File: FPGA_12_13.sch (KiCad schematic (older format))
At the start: 2 parts, among them U1 XC7K160T-FFG676, U51 TXB0104D

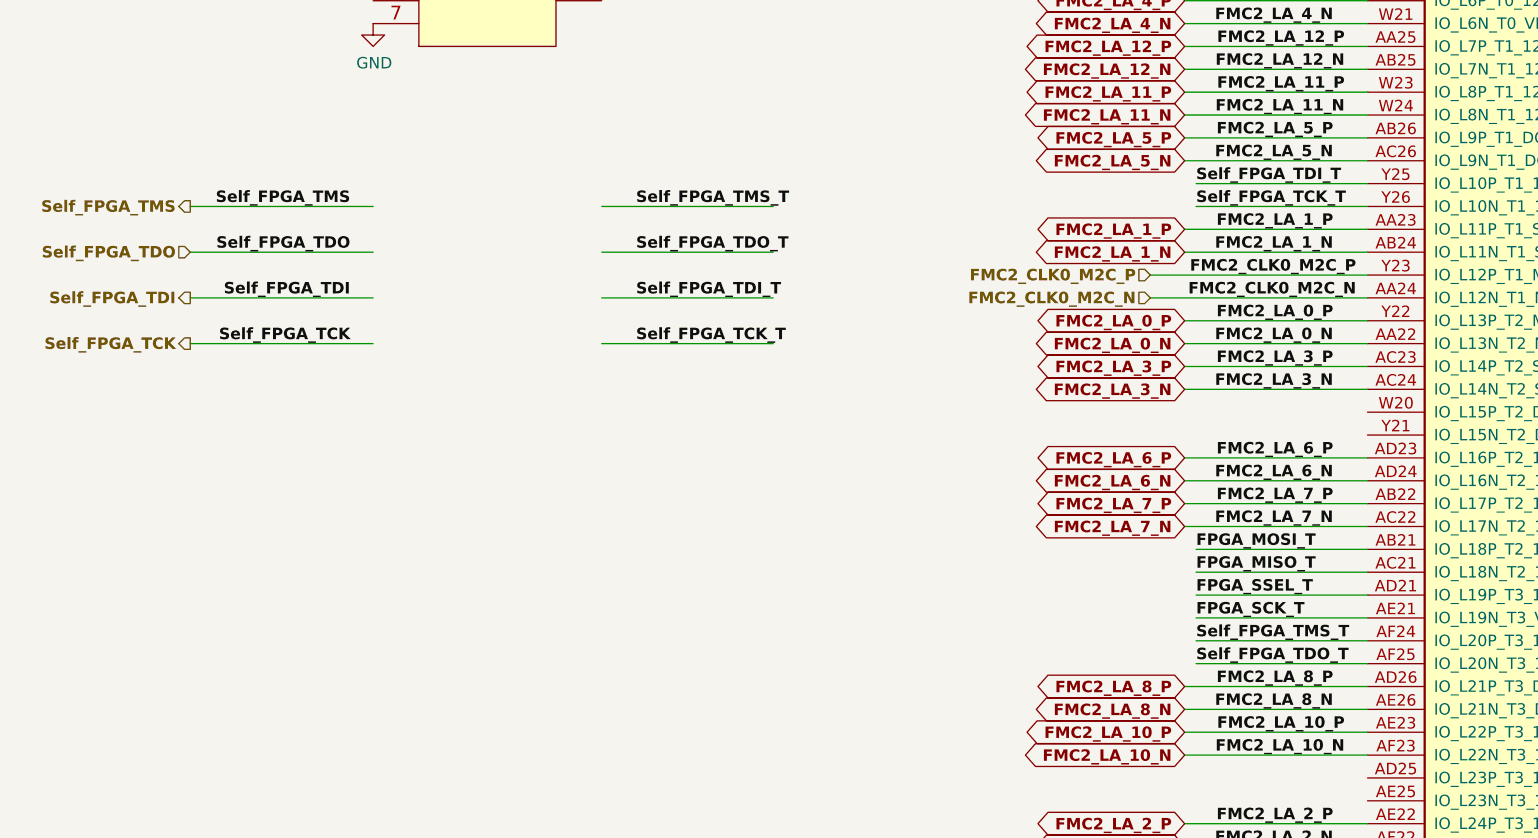
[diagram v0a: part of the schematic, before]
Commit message: MMC routing done
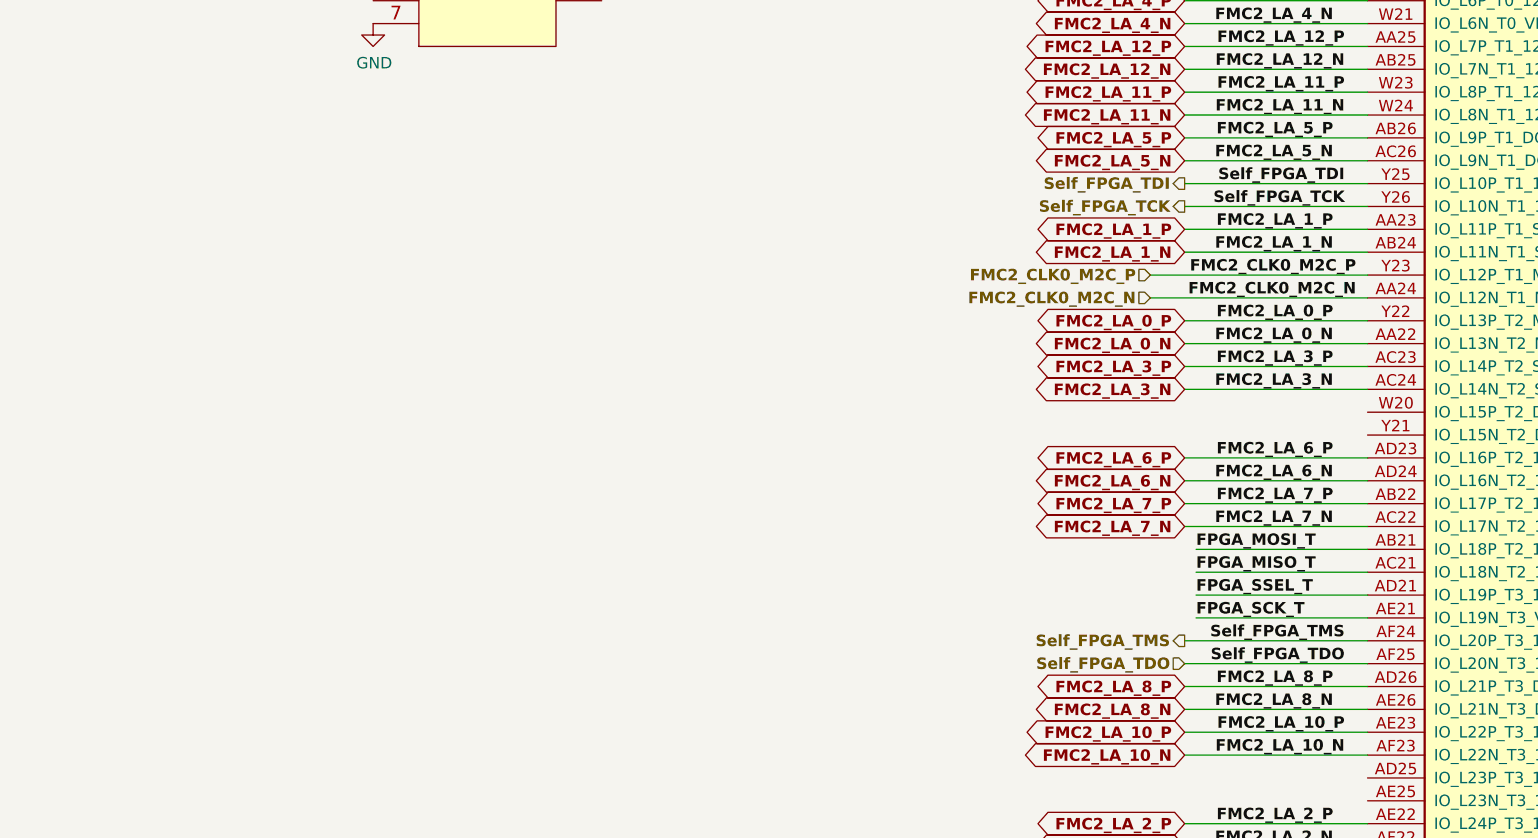
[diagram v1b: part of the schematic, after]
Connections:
- net labels removed: Self_FPGA_TCK_T, Self_FPGA_TDI_T, Self_FPGA_TDO_T, Self_FPGA_TMS_T
- wire segments 165 -> 157
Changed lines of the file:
@@
 Text GLabel 5800 4050 0    50   BiDi ~ 10
 FMC2_LA_16_N
-Text Label 6450 7150 2    50   ~ 10
-FMC2_LA_8_P
 Text Label 6450 7250 2    50   ~ 10
 FMC2_LA_8_N
@@
 Text Label 3400 3950 0    50   ~ 10
 FPGA_SCK_T
-Text Label 3400 5050 0    50   ~ 10
-Self_FPGA_TMS_T
-Text Label 3400 5250 0    50   ~ 10
-Self_FPGA_TDO_T
-Text Label 3400 5450 0    50   ~ 10
-Self_FPGA_TDI_T
-Text Label 3400 5650 0    50   ~ 10
-Self_FPGA_TCK_T
-Wire Wire Line
-	4000 5050 3250 5050
-Wire Wire Line
-	4000 5250 3250 5250
-Wire Wire Line
-	4000 5450 3250 5450
-Wire Wire Line
-	4000 5650 3250 5650
 Wire Wire Line
 	3250 3550 4000 3550
@@
 Text Label 5850 6850 0    50   ~ 10
 FPGA_SCK_T
-Text Label 5850 6950 0    50   ~ 10
-Self_FPGA_TMS_T
-Text Label 5850 7050 0    50   ~ 10
-Self_FPGA_TDO_T
-Text Label 5850 4950 0    50   ~ 10
-Self_FPGA_TDI_T
-Text Label 5850 5050 0    50   ~ 10
-Self_FPGA_TCK_T
-Wire Wire Line
-	6600 6950 5850 6950
-Wire Wire Line
-	6600 7050 5850 7050
-Wire Wire Line
-	6600 4950 5850 4950
-Wire Wire Line
-	6600 5050 5850 5050
 Wire Wire Line
 	5850 6650 6600 6650
@@
 Text HLabel 1450 3350 0    50   Output ~ 10
 FPGA_MOSI
-Text Label 2150 5050 2    50   ~ 10
+Text Label 6500 6950 2    50   ~ 10
 Self_FPGA_TMS
-Text Label 2150 5250 2    50   ~ 10
+Text Label 6500 7050 2    50   ~ 10
 Self_FPGA_TDO
-Text Label 2150 5450 2    50   ~ 10
+Text Label 6500 4950 2    50   ~ 10
 Self_FPGA_TDI
-Text Label 2150 5650 2    50   ~ 10
+Text Label 6500 5050 2    50   ~ 10
 Self_FPGA_TCK
-Text HLabel 1450 5050 0    50   Output ~ 10
+Text HLabel 5800 6950 0    50   Output ~ 10
 Self_FPGA_TMS
-Text HLabel 1450 5250 0    50   Input ~ 10
+Text HLabel 5800 7050 0    50   Input ~ 10
 Self_FPGA_TDO
-Text HLabel 1450 5450 0    50   Output ~ 10
+Text HLabel 5800 4950 0    50   Output ~ 10
 Self_FPGA_TDI
-Text HLabel 1450 5650 0    50   Output ~ 10
+Text HLabel 5800 5050 0    50   Output ~ 10
 Self_FPGA_TCK
 Wire Wire Line
-	1450 5050 2250 5050
-Wire Wire Line
-	1450 5250 2250 5250
-Wire Wire Line
-	1450 5450 2250 5450
-Wire Wire Line
-	1450 5650 2250 5650
+	5800 6950 6600 6950
+Wire Wire Line
+	5800 7050 6600 7050
+Wire Wire Line
+	5800 4950 6600 4950
+Wire Wire Line
+	5800 5050 6600 5050
 Wire Wire Line
 	1450 3350 2250 3350
@@
 	1    0    0    -1
 $EndComp
+Text Label 6450 7150 2    50   ~ 10
+FMC2_LA_8_P
 $EndSCHEMATC

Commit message: clk switch power supply and general routing
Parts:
- added C320, C321: CC0201_100NF_6.3V_10%_X5R, CAPC0603X33N, symbol Capacitors_SMD:CC0201_100NF_6.3V_10%_X5R
- added R8: R0402_0R_JUMPER, Resistors SMD:RESC1005X40N, symbol Resistors_SMD:R0402_0R_JUMPER
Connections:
- net labels added: +3V3
- wire segments 157 -> 166

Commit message: routing done
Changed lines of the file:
@@
 Text Label 6450 5650 2    50   ~ 10
 FMC2_LA_0_N
-Text Label 6450 5750 2    50   ~ 10
+Text Label 6450 7150 2    50   ~ 10
 FMC2_LA_3_P
 Text Label 6450 4750 2    50   ~ 10
@@
 Text Label 6500 3150 2    50   ~ 10
 FMC2_LA_15_P
-Text Label 6450 5850 2    50   ~ 10
+Text Label 6450 7250 2    50   ~ 10
 FMC2_LA_3_N
 Text Label 6450 4850 2    50   ~ 10
@@
 	5800 7850 6600 7850
 Wire Wire Line
-	5800 5750 6600 5750
-Wire Wire Line
-	5800 5850 6600 5850
+	5800 7150 6600 7150
+Wire Wire Line
+	5800 7250 6600 7250
 Wire Wire Line
 	5800 4750 6600 4750
@@
 Text GLabel 5800 7850 0    50   BiDi ~ 10
 FMC2_LA_2_N
-Text GLabel 5800 5750 0    50   BiDi ~ 10
+Text GLabel 5800 7150 0    50   BiDi ~ 10
 FMC2_LA_3_P
-Text GLabel 5800 5850 0    50   BiDi ~ 10
+Text GLabel 5800 7250 0    50   BiDi ~ 10
 FMC2_LA_3_N
 Text GLabel 5800 4750 0    50   BiDi ~ 10
@@
 Text GLabel 5800 4050 0    50   BiDi ~ 10
 FMC2_LA_16_N
-Text Label 6450 7250 2    50   ~ 10
-FMC2_LA_8_N
-Wire Wire Line
-	5800 7150 6600 7150
-Wire Wire Line
-	5800 7250 6600 7250
-Text GLabel 5800 7150 0    50   BiDi ~ 10
-FMC2_LA_8_P
-Text GLabel 5800 7250 0    50   BiDi ~ 10
-FMC2_LA_8_N
 Wire Wire Line
 	5800 3150 6600 3150
@@
 	1    0    0    -1
 $EndComp
-Text Label 6450 7150 2    50   ~ 10
-FMC2_LA_8_P
 $Comp
 L Resistors_SMD:R0402_0R_JUMPER R?
@@
 	3400 4150 3250 4150
 Connection ~ 3400 4150
+Text Label 6450 5850 2    50   ~ 10
+FMC2_LA_8_N
+Wire Wire Line
+	5800 5750 6600 5750
+Wire Wire Line
+	5800 5850 6600 5850
+Text GLabel 5800 5750 0    50   BiDi ~ 10
+FMC2_LA_8_P
+Text GLabel 5800 5850 0    50   BiDi ~ 10
+FMC2_LA_8_N
+Text Label 6450 5750 2    50   ~ 10
+FMC2_LA_8_P
 $EndSCHEMATC

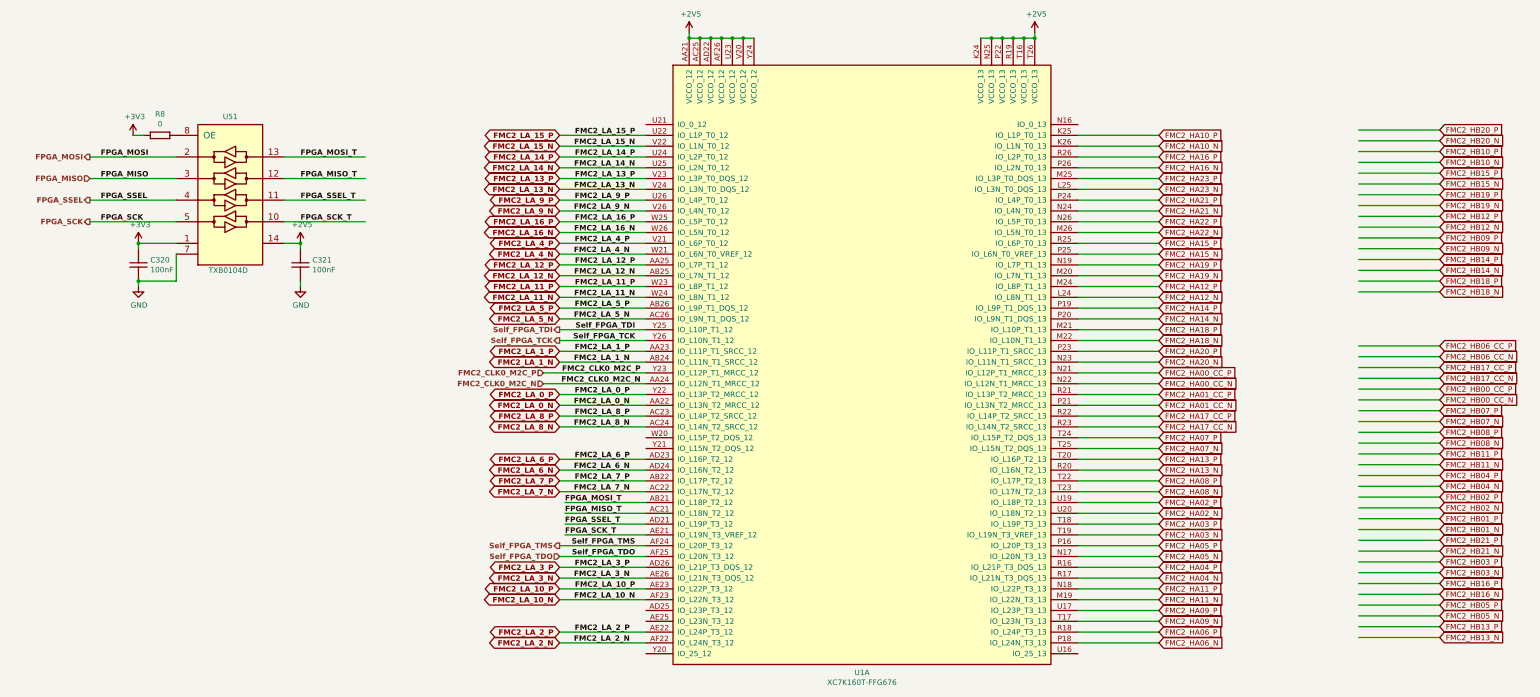
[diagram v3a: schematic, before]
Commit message: DDR lenght mached, 2 additional LEDs added, I2C pullups voltage changed and other minor changes
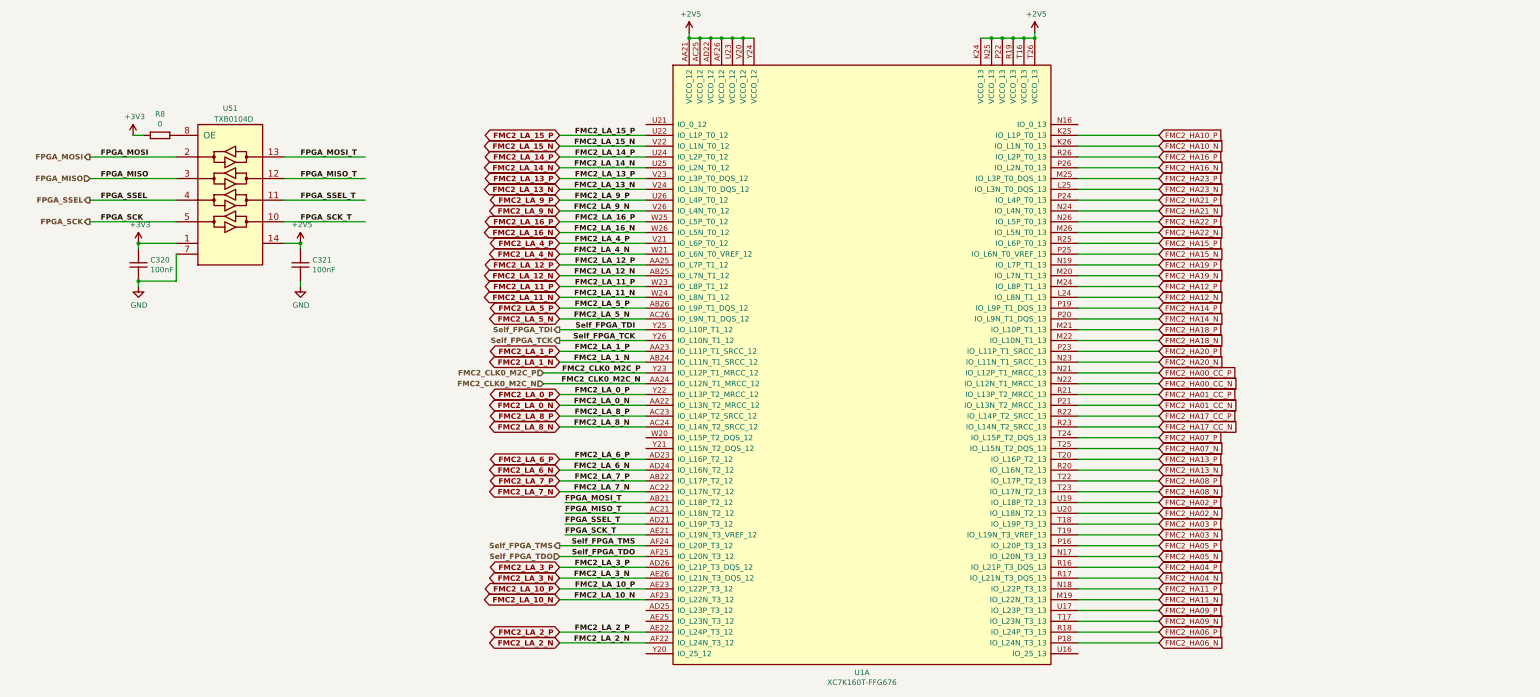
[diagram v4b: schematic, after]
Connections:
- net labels removed: FMC2_HB00_CC_N, FMC2_HB00_CC_P, FMC2_HB01_N, FMC2_HB01_P, FMC2_HB02_N, FMC2_HB02_P, FMC2_HB03_N, FMC2_HB03_P, FMC2_HB04_N, FMC2_HB04_P, FMC2_HB05_N, FMC2_HB05_P, FMC2_HB06_CC_N, FMC2_HB06_CC_P, FMC2_HB07_N, FMC2_HB07_P, FMC2_HB08_N, FMC2_HB08_P, FMC2_HB09_N, FMC2_HB09_P, FMC2_HB10_N, FMC2_HB10_P, FMC2_HB11_N, FMC2_HB11_P, FMC2_HB12_N, FMC2_HB12_P, FMC2_HB13_N, FMC2_HB13_P, FMC2_HB14_N, FMC2_HB14_P, FMC2_HB15_N, FMC2_HB15_P, FMC2_HB16_N, FMC2_HB16_P, FMC2_HB17_CC_N, FMC2_HB17_CC_P, FMC2_HB18_N, FMC2_HB18_P, FMC2_HB19_N, FMC2_HB19_P, FMC2_HB20_N, FMC2_HB20_P, FMC2_HB21_N, FMC2_HB21_P
- wire segments 166 -> 122
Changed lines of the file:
@@
 	1    0    0    -1
 $EndComp
-Wire Wire Line
-	13950 7100 13200 7100
-Wire Wire Line
-	13950 7200 13200 7200
-Wire Wire Line
-	13950 7500 13200 7500
-Wire Wire Line
-	13950 7600 13200 7600
-Wire Wire Line
-	13950 4100 13200 4100
-Wire Wire Line
-	13950 4200 13200 4200
-Wire Wire Line
-	13950 7700 13200 7700
-Wire Wire Line
-	13950 7800 13200 7800
-Wire Wire Line
-	13950 3700 13200 3700
-Wire Wire Line
-	13950 3800 13200 3800
-Text GLabel 13950 7100 2    50   Input ~ 0
-FMC2_HB03_P
-Text GLabel 13950 7200 2    50   Input ~ 0
-FMC2_HB03_N
-Text GLabel 13950 7500 2    50   Input ~ 0
-FMC2_HB05_P
-Text GLabel 13950 7600 2    50   Input ~ 0
-FMC2_HB05_N
-Text GLabel 13950 4100 2    50   Input ~ 0
-FMC2_HB09_P
-Text GLabel 13950 4200 2    50   Input ~ 0
-FMC2_HB09_N
-Text GLabel 13950 7700 2    50   Input ~ 0
-FMC2_HB13_P
-Text GLabel 13950 7800 2    50   Input ~ 0
-FMC2_HB13_N
-Text GLabel 13950 3700 2    50   Input ~ 0
-FMC2_HB19_P
-Text GLabel 13950 3800 2    50   Input ~ 0
-FMC2_HB19_N
-Wire Wire Line
-	13950 6500 13200 6500
-Wire Wire Line
-	13950 6600 13200 6600
-Wire Wire Line
-	13950 6300 13200 6300
-Wire Wire Line
-	13950 6400 13200 6400
-Wire Wire Line
-	13950 5900 13200 5900
-Wire Wire Line
-	13950 6000 13200 6000
-Wire Wire Line
-	13950 3900 13200 3900
-Wire Wire Line
-	13950 4000 13200 4000
-Wire Wire Line
-	13950 7300 13200 7300
-Wire Wire Line
-	13950 7400 13200 7400
-Wire Wire Line
-	13950 3100 13200 3100
-Wire Wire Line
-	13950 3200 13200 3200
-Text GLabel 13950 6500 2    50   Input ~ 0
-FMC2_HB02_P
-Text GLabel 13950 6600 2    50   Input ~ 0
-FMC2_HB02_N
-Text GLabel 13950 6300 2    50   Input ~ 0
-FMC2_HB04_P
-Text GLabel 13950 6400 2    50   Input ~ 0
-FMC2_HB04_N
-Text GLabel 13950 5900 2    50   Input ~ 0
-FMC2_HB08_P
-Text GLabel 13950 6000 2    50   Input ~ 0
-FMC2_HB08_N
-Text GLabel 13950 3900 2    50   Input ~ 0
-FMC2_HB12_P
-Text GLabel 13950 4000 2    50   Input ~ 0
-FMC2_HB12_N
-Text GLabel 13950 7300 2    50   Input ~ 0
-FMC2_HB16_P
-Text GLabel 13950 7400 2    50   Input ~ 0
-FMC2_HB16_N
-Text GLabel 13950 3100 2    50   Input ~ 0
-FMC2_HB20_P
-Text GLabel 13950 3200 2    50   Input ~ 0
-FMC2_HB20_N
-Wire Wire Line
-	13950 6700 13200 6700
-Wire Wire Line
-	13950 6800 13200 6800
-Wire Wire Line
-	13950 5700 13200 5700
-Wire Wire Line
-	13950 5800 13200 5800
-Wire Wire Line
-	13950 6100 13200 6100
-Wire Wire Line
-	13950 6200 13200 6200
-Wire Wire Line
-	13950 3500 13200 3500
-Wire Wire Line
-	13950 3600 13200 3600
-Text GLabel 13950 6700 2    50   Input ~ 0
-FMC2_HB01_P
-Text GLabel 13950 6800 2    50   Input ~ 0
-FMC2_HB01_N
-Text GLabel 13950 5700 2    50   Input ~ 0
-FMC2_HB07_P
-Text GLabel 13950 5800 2    50   Input ~ 0
-FMC2_HB07_N
-Text GLabel 13950 6100 2    50   Input ~ 0
-FMC2_HB11_P
-Text GLabel 13950 6200 2    50   Input ~ 0
-FMC2_HB11_N
-Text GLabel 13950 3500 2    50   Input ~ 0
-FMC2_HB15_P
-Text GLabel 13950 3600 2    50   Input ~ 0
-FMC2_HB15_N
-Wire Wire Line
-	13950 5500 13200 5500
-Wire Wire Line
-	13950 5600 13200 5600
-Wire Wire Line
-	13950 5100 13200 5100
-Wire Wire Line
-	13950 5200 13200 5200
-Wire Wire Line
-	13950 3300 13200 3300
-Wire Wire Line
-	13950 3400 13200 3400
-Wire Wire Line
-	13950 5300 13200 5300
-Wire Wire Line
-	13950 5400 13200 5400
-Text GLabel 13950 5500 2    50   Input ~ 0
-FMC2_HB00_CC_P
-Text GLabel 13950 5600 2    50   Input ~ 0
-FMC2_HB00_CC_N
-Text GLabel 13950 5100 2    50   Input ~ 0
-FMC2_HB06_CC_P
-Text GLabel 13950 5200 2    50   Input ~ 0
-FMC2_HB06_CC_N
-Text GLabel 13950 3300 2    50   Input ~ 0
-FMC2_HB10_P
-Text GLabel 13950 3400 2    50   Input ~ 0
-FMC2_HB10_N
-Text GLabel 13950 5300 2    50   Input ~ 0
-FMC2_HB17_CC_P
-Text GLabel 13950 5400 2    50   Input ~ 0
-FMC2_HB17_CC_N
-Text GLabel 13950 7000 2    50   Input ~ 0
-FMC2_HB21_N
-Text GLabel 13950 6900 2    50   Input ~ 0
-FMC2_HB21_P
-Wire Wire Line
-	13950 7000 13200 7000
-Wire Wire Line
-	13950 6900 13200 6900
 $Comp
 L power:+2V5 #PWR?
@@
 Wire Wire Line
 	10100 2250 10200 2250
-Text GLabel 13950 4600 2    50   Input ~ 0
-FMC2_HB18_N
-Text GLabel 13950 4500 2    50   Input ~ 0
-FMC2_HB18_P
-Wire Wire Line
-	13950 4600 13200 4600
-Wire Wire Line
-	13950 4500 13200 4500
-Text GLabel 13950 4400 2    50   Input ~ 0
-FMC2_HB14_N
-Text GLabel 13950 4300 2    50   Input ~ 0
-FMC2_HB14_P
-Wire Wire Line
-	13950 4400 13200 4400
-Wire Wire Line
-	13950 4300 13200 4300
 Text HLabel 5650 5350 0    50   Input ~ 10
 FMC2_CLK0_M2C_P
@@
 U 1 1 640BB4BE
 P 2450 3050
-F 0 "U51" H 2750 3123 50  0000 C CNN
-F 1 "TXB0104D" H 2550 1700 50  0000 L CNN
+F 0 "U51" H 2750 3200 50  0000 C CNN
+F 1 "TXB0104D" H 2600 3100 50  0000 L CNN
 F 2 "ICs And Semiconductors SMD:SOIC127P600X175-14N" H 2450 1500 50  0001 L CNN
 F 3 " " H 2450 1425 50  0001 L CNN

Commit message: PN updated for some components, README_fab.txt updated
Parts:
- U1: value XC7K160T-FFG676 -> XC7K160T-2FFG676C
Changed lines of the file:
@@
 AR Path="/5C907554/5F569040/5F597EC7" Ref="U1"  Part="1"
 F 0 "U1" H 8600 2175 50  0000 C CNN
-F 1 "XC7K160T-FFG676" H 8600 2084 50  0000 C CNN
+F 1 "XC7K160T-2FFG676C" H 8600 2084 50  0000 C CNN
 F 2 "ICs And Semiconductors SMD_BGA:BGA676C100P26X26_2700X2700X260" H 8600 5150 50  0001 C CNN
 F 3 "" H 8600 5150 50  0000 C CNN

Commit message: Automated edit to move cache / rescue symbols to actual eeschem library
Results of running dissect_lib3.py, not posted here
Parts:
- U1: symbol FPGA_Xilinx_Kintex7:XC7K160T-FFG676 -> marble_misc:XC7K160T-FFG676
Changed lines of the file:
@@
 $EndDescr
 $Comp
-L FPGA_Xilinx_Kintex7:XC7K160T-FFG676 U?
+L marble_misc:XC7K160T-FFG676 U?
 U 1 1 5F597EC7
 P 8600 5150

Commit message: 16 warnings, 16 errors
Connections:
- no-connect marks 0 -> 8
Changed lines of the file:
@@
 Text Label 6450 5750 2    50   ~ 10
 FMC2_LA_8_P
+NoConn ~ 6600 7550
+NoConn ~ 6600 7650
+NoConn ~ 6600 7950
+NoConn ~ 6600 6050
+NoConn ~ 6600 5950
+NoConn ~ 6600 3050
+NoConn ~ 10600 3050
+NoConn ~ 10600 7950
 $EndSCHEMATC

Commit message: Tweak Resistor attributes to improve BOM output
Clean according to KiBoM and non_generic.py
Still a metric ton of buried inconsistencies
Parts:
- R8: footprint Resistors SMD:RESC1005X40N -> RESC1005X40N; Comment 0 -> =Value; Library Name Resistors.DbLib -> Resistors SMD
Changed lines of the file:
@@
 F 0 "R8" H 2100 3347 50  0000 C CNN
 F 1 "R0402_0R_JUMPER" H 1950 2955 50  0001 L CNN
-F 2 "Resistors SMD:RESC1005X40N" H 1950 2880 50  0001 L CNN
+F 2 "RESC1005X40N" H 1950 2880 50  0001 L CNN
 F 3 " " H 1950 2805 50  0001 L CNN
 F 4 "0" H 2100 3256 50  0000 C CNN "Val"
@@
 F 6 "Resistor" H 1950 2655 50  0001 L CNN "Library Ref"
 F 7 "SchLib\\Resistors.SchLib" H 1950 2580 50  0001 L CNN "Library Path"
-F 8 "0" H 1950 2505 50  0001 L CNN "Comment"
+F 8 "=Value" H 1950 2505 50  0001 L CNN "Comment"
 F 9 "Standard" H 1950 2430 50  0001 L CNN "Component Kind"
 F 10 "Standard" H 1950 2355 50  0001 L CNN "Component Type"
@@
 F 37 "10/17/12 00:00:00" H 1950 330 50  0001 L CNN "LatestRevisionDate"
 F 38 "Resistors SMD" H 1950 255 50  0001 L CNN "Database Table Name"
-F 39 "Resistors.DbLib" H 1950 180 50  0001 L CNN "Library Name"
+F 39 "Resistors SMD" H 1950 180 50  0001 L CNN "Library Name"
 F 40 "Resistors SMD" H 1950 105 50  0001 L CNN "Footprint Library"
 F 41 "This work is licensed under the Creative Commons CC-BY-SA 4.0 License. To the extent that circuit schematics that use Licensed Material can be considered to be ‘Adapted Material’, then the copyright holder waives article 3.b of the license with respect to these schematics." H 1950 30  50  0001 L CNN "License"
